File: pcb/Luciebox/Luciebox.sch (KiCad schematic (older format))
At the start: 42 parts, among them J1 Screw_Terminal_01x07, J2 Screw_Terminal_01x07, J3 Screw_Terminal_01x07, J4 Screw_Terminal_01x07, P1 CONN_01X01, P2 CONN_01X01, P3 CONN_01X01, P4 CONN_01X01, P5 Digital, P6 Power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

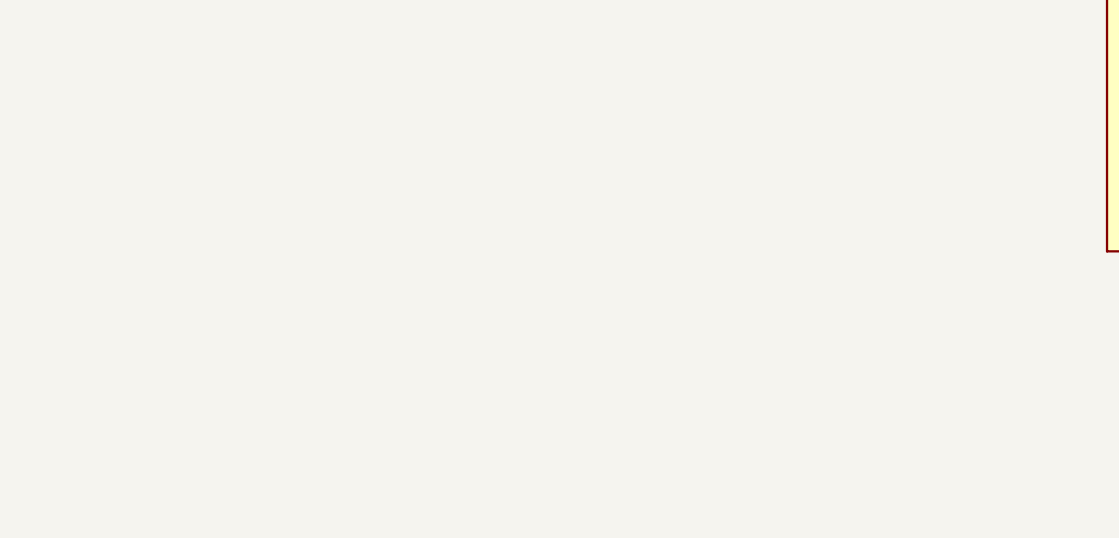
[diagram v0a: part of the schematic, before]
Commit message: pcb add auto power OFF hardware
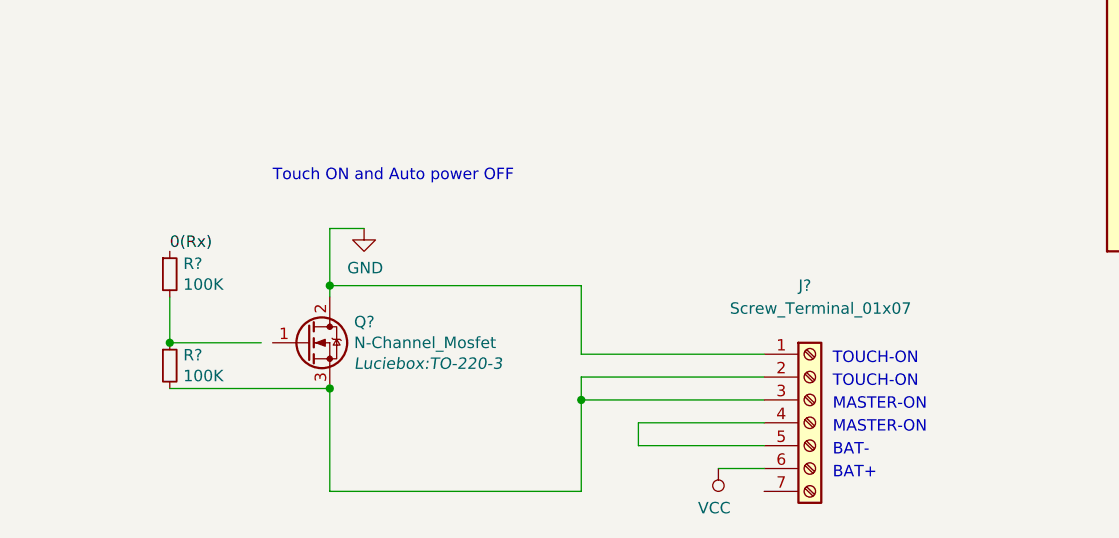
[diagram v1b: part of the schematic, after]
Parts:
- added J?: Screw_Terminal_01x07, Luciebox:Terminal_7x1_100mil, symbol Connector:Screw_Terminal_01x07
- added Q?: N-Channel_Mosfet, Luciebox:TO-220-3, symbol Luciebox_components:N-Channel_Mosfet
- added R? (x2): 100K, Luciebox:1206, symbol Device:R_Small
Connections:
- net 0(Rx): now also R?.1
- net GND: now also J?.1 (Pin_1), Q?.2 (D)
- net VCC: now also J?.6 (Pin_6)
- new net: J?.2 (Pin_2), J?.3 (Pin_3), Q?.3 (S), R?.2
- new net: R?.1, R?.2
- new net: J?.4 (Pin_4), J?.5 (Pin_5)
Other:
- note added: "BAT+"
- note added: "BAT-"
- note added: "MASTER-ON"
- note added: "TOUCH-ON"
- note added: "Touch ON and Auto power OFF"
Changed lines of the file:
@@
 EESchema Schematic File Version 4
 LIBS:Luciebox-cache
-LIBS:R-2R_DAC-cache
 EELAYER 29 0
 EELAYER END
@@
 Wire Wire Line
 	9250 5250 8500 5250
+$Comp
+L Luciebox_components:N-Channel_Mosfet Q?
+U 1 1 5D6BDEDC
+P 3900 6750
+F 0 "Q?" H 4106 6841 50  0000 L CNN
+F 1 "N-Channel_Mosfet" H 4106 6750 50  0000 L CNN
+F 2 "Luciebox:TO-220-3" H 4106 6659 50  0000 L CIN
+F 3 "https://www.onsemi.com/pub/Collateral/FQP30N06L-D.pdf" V 3900 6750 50  0001 L CNN
+	1    3900 6750
+	1    0    0    -1
+$EndComp
+$Comp
+L Device:R_Small R?
+U 1 1 5D6C3437
+P 3300 6450
+F 0 "R?" H 3359 6496 50  0000 L CNN
+F 1 "100K" H 3359 6405 50  0000 L CNN
+F 2 "Luciebox:1206" H 3300 6450 50  0001 C CNN
+F 3 "~" H 3300 6450 50  0001 C CNN
+	1    3300 6450
+	1    0    0    -1
+$EndComp
+$Comp
+L Device:R_Small R?
+U 1 1 5D6C3ACD
+P 3300 6850
+F 0 "R?" H 3359 6896 50  0000 L CNN
+F 1 "100K" H 3359 6805 50  0000 L CNN
+F 2 "Luciebox:1206" H 3300 6850 50  0001 C CNN
+F 3 "~" H 3300 6850 50  0001 C CNN
+	1    3300 6850
+	1    0    0    -1
+$EndComp
+Wire Wire Line
+	3700 6750 3300 6750
+Wire Wire Line
+	3300 6550 3300 6750
+Connection ~ 3300 6750
+Text Label 3300 6350 0    50   ~ 0
+0(Rx)
+$Comp
+L power:GND #PWR?
+U 1 1 5D70EC69
+P 4150 6250
+F 0 "#PWR?" H 4150 6000 50  0001 C CNN
+F 1 "GND" H 4155 6077 50  0000 C CNN
+F 2 "" H 4150 6250 50  0001 C CNN
+F 3 "" H 4150 6250 50  0001 C CNN
+	1    4150 6250
+	1    0    0    -1
+$EndComp
+Wire Wire Line
+	4000 6950 3300 6950
+Wire Wire Line
+	4150 6250 4000 6250
+Wire Wire Line
+	4000 6250 4000 6500
+Wire Wire Line
+	4000 6950 4000 7400
+Connection ~ 4000 6950
+$Comp
+L Connector:Screw_Terminal_01x07 J?
+U 1 1 5D74D272
+P 6100 7100
+F 0 "J?" H 6050 7700 50  0000 L CNN
+F 1 "Screw_Terminal_01x07" H 5750 7600 50  0000 L CNN
+F 2 "Luciebox:Terminal_7x1_100mil" H 6100 7100 50  0001 C CNN
+F 3 "~" H 6100 7100 50  0001 C CNN
+	1    6100 7100
+	1    0    0    -1
+$EndComp
+Wire Wire Line
+	5100 6500 4000 6500
+Connection ~ 4000 6500
+Wire Wire Line
+	4000 6500 4000 6550
+Wire Wire Line
+	5900 6800 5100 6800
+Wire Wire Line
+	5100 6800 5100 6500
+Wire Wire Line
+	5900 6900 5100 6900
+Wire Wire Line
+	5100 7400 4000 7400
+Wire Wire Line
+	5100 6900 5100 7000
+Wire Wire Line
+	5900 7000 5100 7000
+Connection ~ 5100 7000
+Wire Wire Line
+	5100 7000 5100 7400
+Wire Wire Line
+	5900 7100 5350 7100
+$Comp
+L power:VCC #PWR?
+U 1 1 5D7FF3DB
+P 5700 7300
+F 0 "#PWR?" H 5700 7150 50  0001 C CNN
+F 1 "VCC" H 5718 7473 50  0000 C CNN
+F 2 "" H 5700 7300 50  0001 C CNN
+F 3 "" H 5700 7300 50  0001 C CNN
+	1    5700 7300
+	-1   0    0    1
+$EndComp
+Text Notes 6200 7350 0    50   ~ 0
+BAT+
+Text Notes 6200 7250 0    50   ~ 0
+BAT-
+Text Notes 6200 7050 0    50   ~ 0
+MASTER-ON
+Text Notes 6200 7150 0    50   ~ 0
+MASTER-ON
+Text Notes 6200 6850 0    50   ~ 0
+TOUCH-ON
+Text Notes 6200 6950 0    50   ~ 0
+TOUCH-ON
+Wire Wire Line
+	5350 7200 5350 7100
+Wire Wire Line
+	5350 7200 5900 7200
+Wire Wire Line
+	5900 7300 5700 7300
+Text Notes 3750 6050 0    50   ~ 0
+Touch ON and Auto power OFF
 $EndSCHEMATC

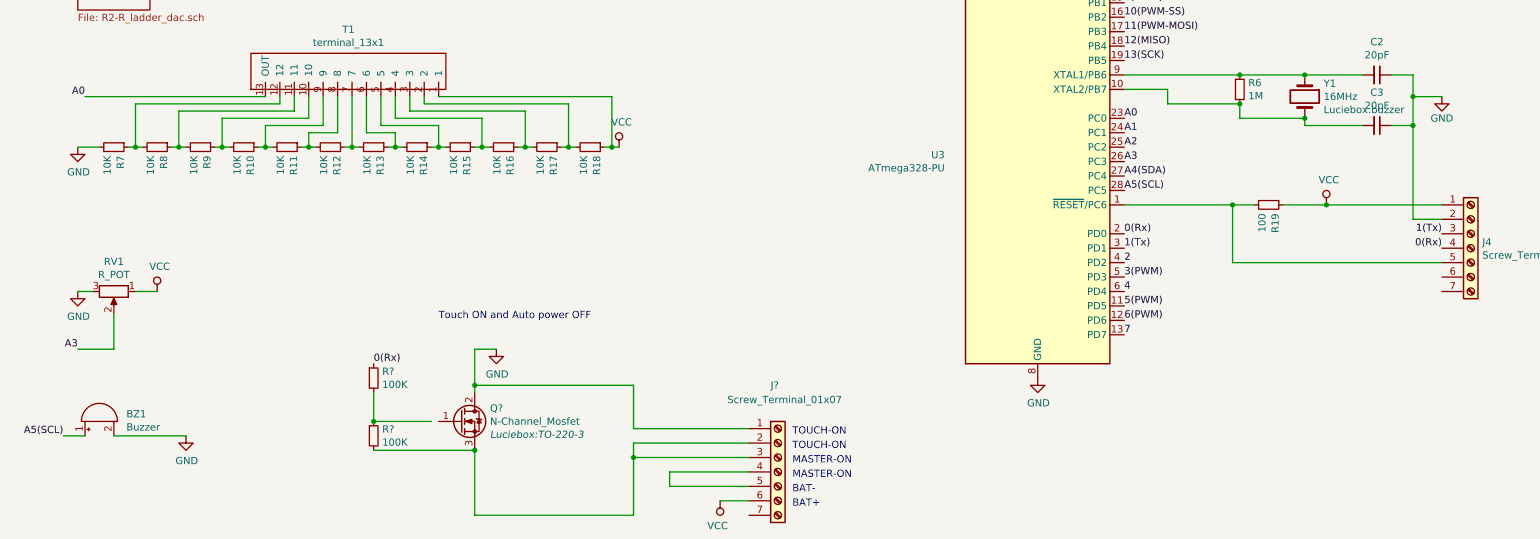
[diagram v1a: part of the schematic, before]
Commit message: all components have footprint. All fitting on board.
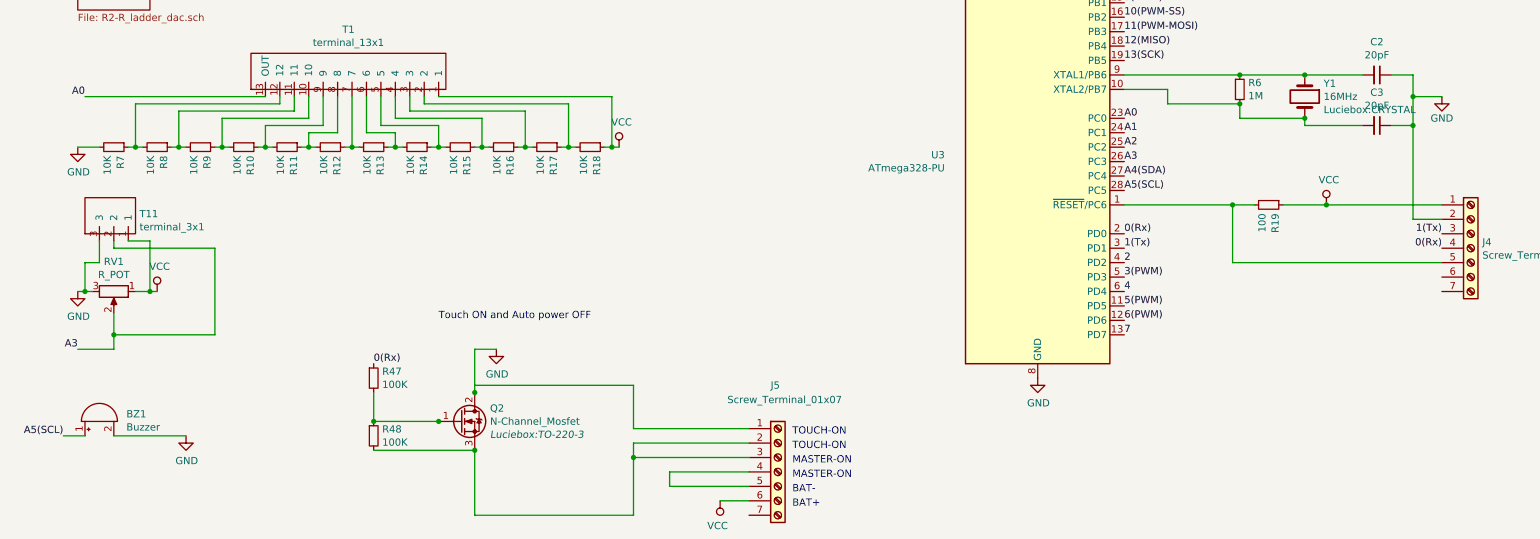
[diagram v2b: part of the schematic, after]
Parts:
- added T11: terminal_3x1, Luciebox:Terminal_3x1_100mil, symbol Luciebox_components:terminal_3x1
- RV1: footprint (none) -> Luciebox:BIG_POTENTIO
- Y1: footprint Luciebox:buzzer -> Luciebox:CRYSTAL
- gave numbers to parts that had none: 4
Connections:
- net A3: now also T11.2
- net GND: now also T11.3
- net VCC: now also T11.1
- net at Q2.1 (G): now also R47.2, R48.1
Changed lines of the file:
@@
 F 0 "RV1" V 1293 5850 50  0000 C CNN
 F 1 "R_POT" V 1384 5850 50  0000 C CNN
-F 2 "" H 1500 5850 50  0001 C CNN
+F 2 "Luciebox:BIG_POTENTIO" H 1500 5850 50  0001 C CNN
 F 3 "~" H 1500 5850 50  0001 C CNN
 	1    1500 5850
@@
 $EndComp
 Wire Wire Line
-	1650 5850 1800 5850
-Wire Wire Line
-	1350 5850 1250 5850
-Wire Wire Line
-	1500 6000 1500 6250
+	1350 5850 1300 5850
+Wire Wire Line
+	1500 6000 1500 6150
 Wire Wire Line
 	1500 6250 1250 6250
@@
 F 0 "Y1" V 9659 4631 50  0000 L CNN
 F 1 "16MHz" V 9750 4631 50  0000 L CNN
-F 2 "Luciebox:buzzer" V 9841 4631 50  0000 L CNN
+F 2 "Luciebox:CRYSTAL" V 9841 4631 50  0000 L CNN
 F 3 "~" H 9750 4500 50  0001 C CNN
 	1    9750 4500
@@
 	9250 5250 8500 5250
 $Comp
-L Luciebox_components:N-Channel_Mosfet Q?
+L Luciebox_components:N-Channel_Mosfet Q2
 U 1 1 5D6BDEDC
 P 3900 6750
-F 0 "Q?" H 4106 6841 50  0000 L CNN
+F 0 "Q2" H 4106 6841 50  0000 L CNN
 F 1 "N-Channel_Mosfet" H 4106 6750 50  0000 L CNN
 F 2 "Luciebox:TO-220-3" H 4106 6659 50  0000 L CIN
@@
 $EndComp
 $Comp
-L Device:R_Small R?
+L Device:R_Small R47
 U 1 1 5D6C3437
 P 3300 6450
-F 0 "R?" H 3359 6496 50  0000 L CNN
+F 0 "R47" H 3359 6496 50  0000 L CNN
 F 1 "100K" H 3359 6405 50  0000 L CNN
 F 2 "Luciebox:1206" H 3300 6450 50  0001 C CNN
@@
 $EndComp
 $Comp
-L Device:R_Small R?
+L Device:R_Small R48
 U 1 1 5D6C3ACD
 P 3300 6850
-F 0 "R?" H 3359 6896 50  0000 L CNN
+F 0 "R48" H 3359 6896 50  0000 L CNN
 F 1 "100K" H 3359 6805 50  0000 L CNN
 F 2 "Luciebox:1206" H 3300 6850 50  0001 C CNN
@@
 $EndComp
 Wire Wire Line
-	3700 6750 3300 6750
-Wire Wire Line
 	3300 6550 3300 6750
 Connection ~ 3300 6750
@@
 0(Rx)
 $Comp
-L power:GND #PWR?
+L power:GND #PWR0101
 U 1 1 5D70EC69
 P 4150 6250
-F 0 "#PWR?" H 4150 6000 50  0001 C CNN
+F 0 "#PWR0101" H 4150 6000 50  0001 C CNN
 F 1 "GND" H 4155 6077 50  0000 C CNN
 F 2 "" H 4150 6250 50  0001 C CNN
@@
 Connection ~ 4000 6950
 $Comp
-L Connector:Screw_Terminal_01x07 J?
+L Connector:Screw_Terminal_01x07 J5
 U 1 1 5D74D272
 P 6100 7100
-F 0 "J?" H 6050 7700 50  0000 L CNN
+F 0 "J5" H 6050 7700 50  0000 L CNN
 F 1 "Screw_Terminal_01x07" H 5750 7600 50  0000 L CNN
 F 2 "Luciebox:Terminal_7x1_100mil" H 6100 7100 50  0001 C CNN
@@
 Wire Wire Line
 	5100 6500 4000 6500
-Connection ~ 4000 6500
+Connection ~ 4000 6550
 Wire Wire Line
 	4000 6500 4000 6550
@@
 	5900 7100 5350 7100
 $Comp
-L power:VCC #PWR?
+L power:VCC #PWR0102
 U 1 1 5D7FF3DB
 P 5700 7300
-F 0 "#PWR?" H 5700 7150 50  0001 C CNN
+F 0 "#PWR0102" H 5700 7150 50  0001 C CNN
 F 1 "VCC" H 5718 7473 50  0000 C CNN
 F 2 "" H 5700 7300 50  0001 C CNN
@@
 Text Notes 3750 6050 0    50   ~ 0
 Touch ON and Auto power OFF
+$Comp
+L Luciebox_components:terminal_3x1 T11
+U 1 1 5DC4B415
+P 1600 5450
+F 0 "T11" V 1738 5372 50  0000 R CNN
+F 1 "terminal_3x1" V 1647 5372 50  0000 R CNN
+F 2 "Luciebox:Terminal_3x1_100mil" H 1400 5350 50  0001 C CNN
+F 3 "" H 1550 5850 50  0001 C CNN
+	1    1600 5450
+	0    -1   -1   0
+$EndComp
+Wire Wire Line
+	1400 5500 1400 5650
+Wire Wire Line
+	1400 5650 1300 5650
+Wire Wire Line
+	1300 5650 1300 5850
+Connection ~ 1300 5850
+Wire Wire Line
+	1300 5850 1250 5850
+Wire Wire Line
+	1600 5500 1750 5500
+Wire Wire Line
+	1750 5500 1750 5850
+Wire Wire Line
+	1750 5850 1800 5850
+Wire Wire Line
+	1500 5500 1500 5550
+Connection ~ 1500 6150
+Wire Wire Line
+	1500 6150 1500 6250
+Wire Wire Line
+	1750 5850 1650 5850
+Connection ~ 1750 5850
+Wire Wire Line
+	2200 5550 2200 6150
+Wire Wire Line
+	1500 5550 2200 5550
+Wire Wire Line
+	1500 6150 2200 6150
+Wire Wire Line
+	3300 6750 3750 6750
+Connection ~ 3750 6750
 $EndSCHEMATC

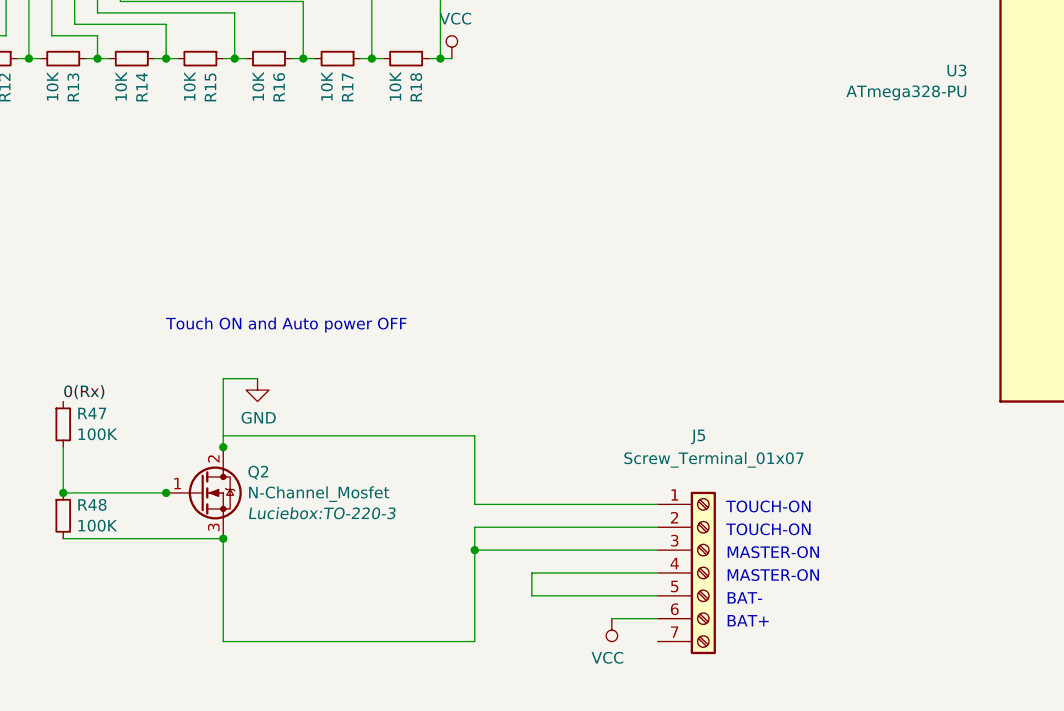
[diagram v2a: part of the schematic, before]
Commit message: pcb all traces made. Copper pours in place. Check for trace widths and artwork.
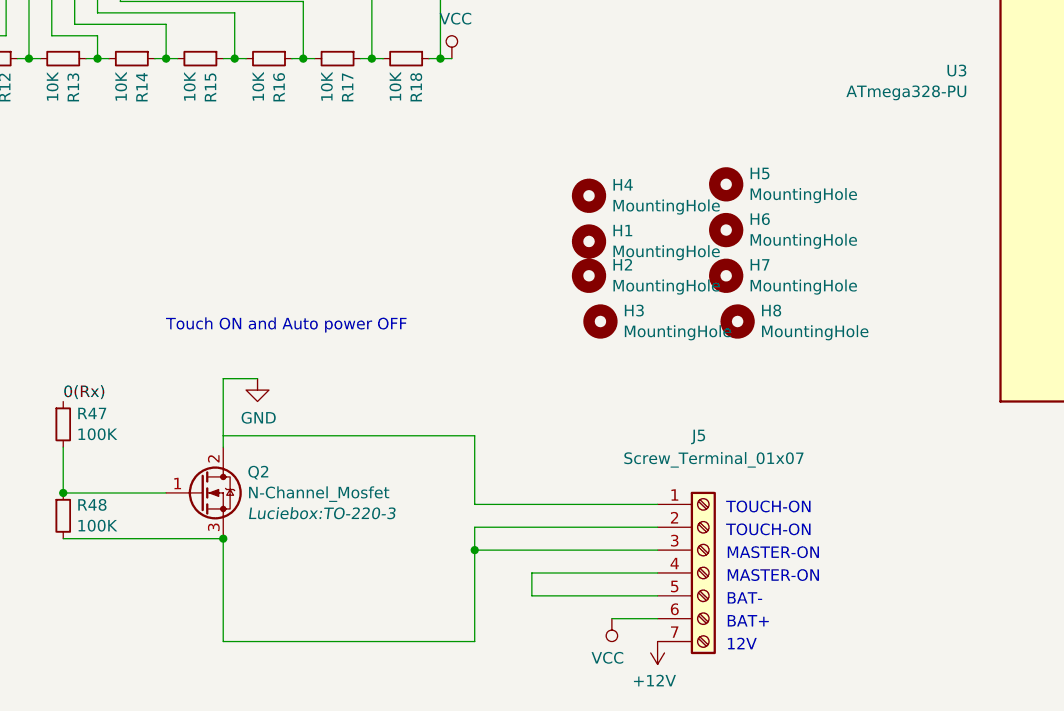
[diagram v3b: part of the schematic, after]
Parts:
- added H1, H2, H3, H4, H5, H6, H7, H8: MountingHole, MountingHole:MountingHole_4mm, symbol Mechanical:MountingHole
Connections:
- net +12V: now also J5.7 (Pin_7)
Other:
- note added: "12V"
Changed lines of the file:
@@
 EESchema Schematic File Version 4
 LIBS:Luciebox-cache
-EELAYER 29 0
+EELAYER 26 0
 EELAYER END
 $Descr A4 11693 8268
@@
 Wire Wire Line
 	5100 6500 4000 6500
-Connection ~ 4000 6550
 Wire Wire Line
 	4000 6500 4000 6550
@@
 Wire Wire Line
 	3300 6750 3750 6750
-Connection ~ 3750 6750
+$Comp
+L power:+12V #PWR0103
+U 1 1 5DC88B13
+P 5900 7400
+F 0 "#PWR0103" H 5900 7250 50  0001 C CNN
+F 1 "+12V" H 5915 7573 50  0000 C CNN
+F 2 "" H 5900 7400 50  0001 C CNN
+F 3 "" H 5900 7400 50  0001 C CNN
+	1    5900 7400
+	-1   0    0    1
+$EndComp
+Text Notes 6200 7450 0    50   ~ 0
+12V
+$Comp
+L Mechanical:MountingHole H4
+U 1 1 5DC89D39
+P 5600 5450
+F 0 "H4" H 5700 5496 50  0000 L CNN
+F 1 "MountingHole" H 5700 5405 50  0000 L CNN
+F 2 "MountingHole:MountingHole_4mm" H 5600 5450 50  0001 C CNN
+F 3 "~" H 5600 5450 50  0001 C CNN
+	1    5600 5450
+	1    0    0    -1
+$EndComp
+$Comp
+L Mechanical:MountingHole H1
+U 1 1 5DC9D1FF
+P 5600 5650
+F 0 "H1" H 5700 5696 50  0000 L CNN
+F 1 "MountingHole" H 5700 5605 50  0000 L CNN
+F 2 "MountingHole:MountingHole_4mm" H 5600 5650 50  0001 C CNN
+F 3 "~" H 5600 5650 50  0001 C CNN
+	1    5600 5650
+	1    0    0    -1
+$EndComp
+$Comp
+L Mechanical:MountingHole H2
+U 1 1 5DC9D279
+P 5600 5800
+F 0 "H2" H 5700 5846 50  0000 L CNN
+F 1 "MountingHole" H 5700 5755 50  0000 L CNN
+F 2 "MountingHole:MountingHole_4mm" H 5600 5800 50  0001 C CNN
+F 3 "~" H 5600 5800 50  0001 C CNN
+	1    5600 5800
+	1    0    0    -1
+$EndComp
+$Comp
+L Mechanical:MountingHole H3
+U 1 1 5DC9D2EF
+P 5650 6000
+F 0 "H3" H 5750 6046 50  0000 L CNN
+F 1 "MountingHole" H 5750 5955 50  0000 L CNN
+F 2 "MountingHole:MountingHole_4mm" H 5650 6000 50  0001 C CNN
+F 3 "~" H 5650 6000 50  0001 C CNN
+	1    5650 6000
+	1    0    0    -1
+$EndComp
+$Comp
+L Mechanical:MountingHole H8
+U 1 1 5DC9D36B
+P 6250 6000
+F 0 "H8" H 6350 6046 50  0000 L CNN
+F 1 "MountingHole" H 6350 5955 50  0000 L CNN
+F 2 "MountingHole:MountingHole_4mm" H 6250 6000 50  0001 C CNN
+F 3 "~" H 6250 6000 50  0001 C CNN
+	1    6250 6000
+	1    0    0    -1
+$EndComp
+$Comp
+L Mechanical:MountingHole H7
+U 1 1 5DC9D403
+P 6200 5800
+F 0 "H7" H 6300 5846 50  0000 L CNN
+F 1 "MountingHole" H 6300 5755 50  0000 L CNN
+F 2 "MountingHole:MountingHole_4mm" H 6200 5800 50  0001 C CNN
+F 3 "~" H 6200 5800 50  0001 C CNN
+	1    6200 5800
+	1    0    0    -1
+$EndComp
+$Comp
+L Mechanical:MountingHole H6
+U 1 1 5DC9D485
+P 6200 5600
+F 0 "H6" H 6300 5646 50  0000 L CNN
+F 1 "MountingHole" H 6300 5555 50  0000 L CNN
+F 2 "MountingHole:MountingHole_4mm" H 6200 5600 50  0001 C CNN
+F 3 "~" H 6200 5600 50  0001 C CNN
+	1    6200 5600
+	1    0    0    -1
+$EndComp
+$Comp
+L Mechanical:MountingHole H5
+U 1 1 5DC9D509
+P 6200 5400
+F 0 "H5" H 6300 5446 50  0000 L CNN
+F 1 "MountingHole" H 6300 5355 50  0000 L CNN
+F 2 "MountingHole:MountingHole_4mm" H 6200 5400 50  0001 C CNN
+F 3 "~" H 6200 5400 50  0001 C CNN
+	1    6200 5400
+	1    0    0    -1
+$EndComp
 $EndSCHEMATC
